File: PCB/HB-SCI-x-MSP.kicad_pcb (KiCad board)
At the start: 2 copper layers, 57 x 24 mm, 27 parts, among them J1 Prog, J2 FTDI, Q1 BC858, SW1 Config, SW2 4x SW, U1 ATmega328P-AU, U2 MSP430F2001IPW, U3 CC1101, Y1 32kHz

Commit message: update PCB
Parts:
- added C6: 12pF, Capacitor_SMD:C_0805_2012Metric_Pad1.15x1.40mm_HandSolder, B.Cu at (91.0, 37.6)
- added C7: 12pF, Capacitor_SMD:C_0805_2012Metric_Pad1.15x1.40mm_HandSolder, B.Cu at (91.0, 39.5)
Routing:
- net Net-(C7-Pad1): track 2.71 -> 4.44 mm
- net Net-(C6-Pad1): track 3.23 -> 4.96 mm

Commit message: update pcb
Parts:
- added C8: 1n, Capacitor_SMD:C_0805_2012Metric_Pad1.15x1.40mm_HandSolder, F.Cu at (74.7, 36.4)
- added R10: 47k, Resistor_SMD:R_0805_2012Metric_Pad1.15x1.40mm_HandSolder, F.Cu at (74.7, 39.1)
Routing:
- net MSP_RST: track 50.3 -> 77.2 mm, vias 2 -> 1
- net AVR_RST: track 61.4 -> 38.3 mm
- net Net-(JP1-Pad2): track 45.2 -> 22.8 mm, vias 0 -> 2
- net RX: track 33.3 -> 49.3 mm, vias 1 -> 0
- net SCK: track 30.7 -> 43.6 mm
- net TX: track 31.8 -> 43.8 mm, vias 1 -> 0
- net MISO: track 34.6 -> 27.5 mm
- net TEST: track 47.8 -> 54.9 mm, vias 2 -> 0
- net +BATT: track 84.8 -> 77.9 mm
- net CS: track 9.08 -> 13.0 mm
- net MOSI: track 48.6 -> 46.6 mm
- net Net-(R1-Pad2): track 39.3 -> 37.7 mm
- net Net-(R3-Pad2): track 16.7 -> 15.0 mm
- net GND: track 97.7 -> 96.4 mm
- net Net-(D2-Pad2): track 25.6 -> 24.9 mm
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
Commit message: update pcb
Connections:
- net MSP_RST renamed TDIO
- net TEST renamed TCK

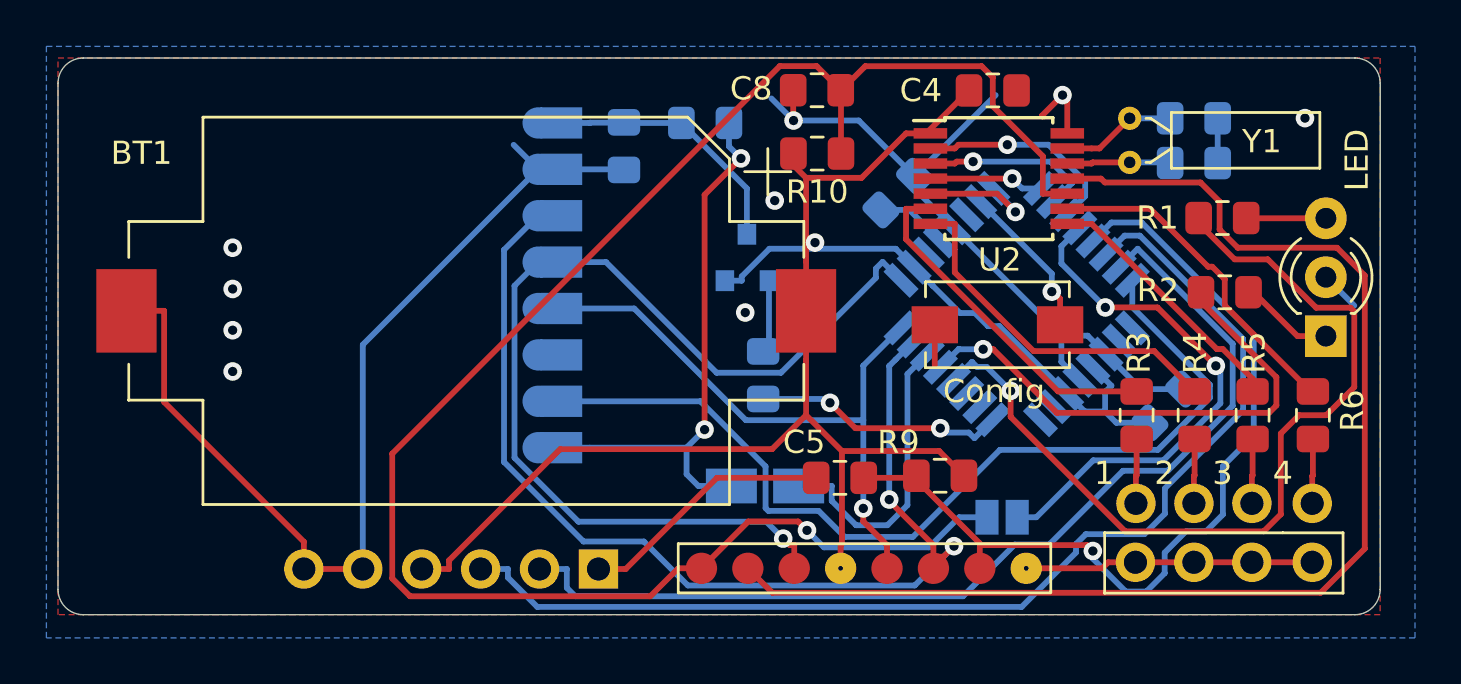
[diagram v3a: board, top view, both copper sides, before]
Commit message: update Kicad 6
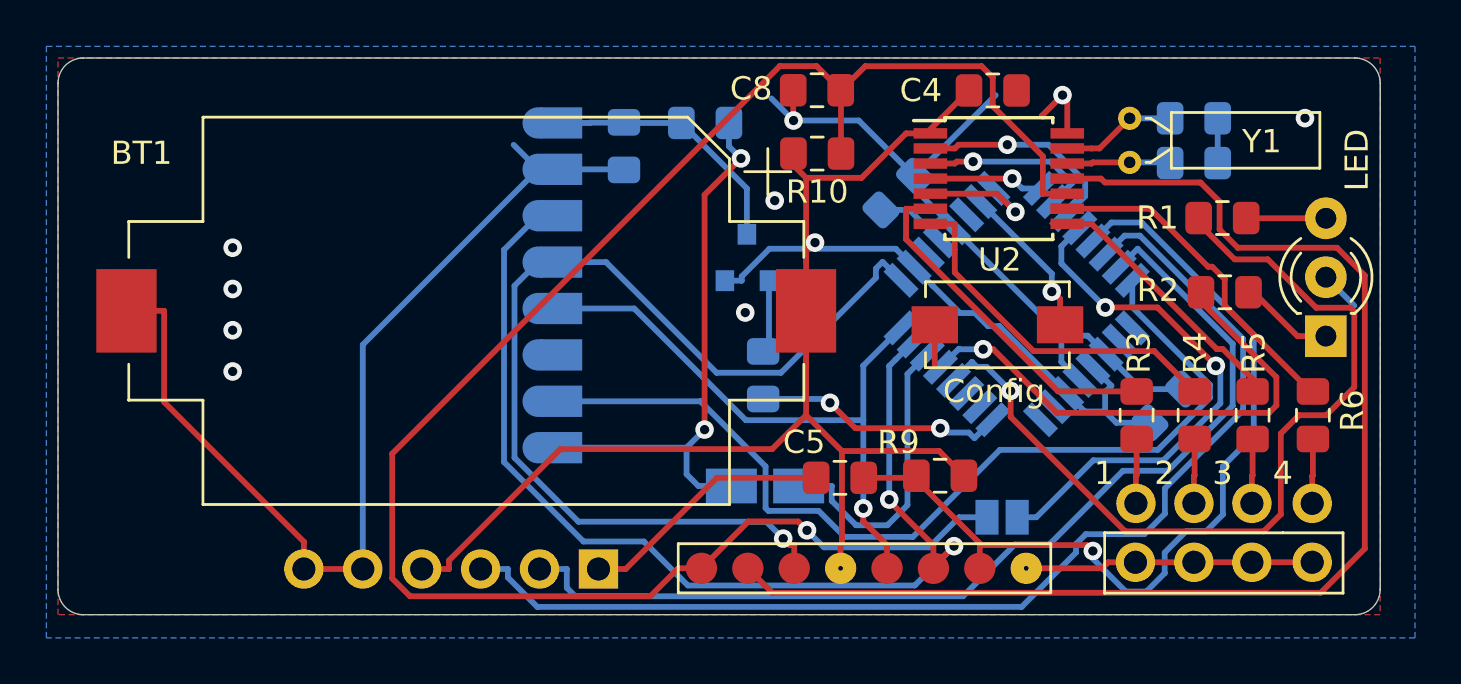
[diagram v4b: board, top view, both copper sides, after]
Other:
- net class Default removed
